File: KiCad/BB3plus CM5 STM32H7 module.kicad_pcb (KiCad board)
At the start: 6 copper layers, 55 x 40 mm, 134 parts, among them IC1 AZ1117CH2-3.3TRG1, IC10 MX25UM25645GXDI00-T, IC2 SN74LVC1G14DBVR, IC3 STM32H7R7L8H6H, IC4 TLV75718PDRVR, IC5 MX52LM04A11XVW, IC6 LAN8742A-CZ-TR, IC7 APS256XXN-OBR-BG, IC8 TFP410PAP, IC9 TS3DV642A0RUAR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

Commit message: DIN3 pin assigned
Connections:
- net UART0_RX/DIN2 renamed UART_RX/DIN2
- net UART0_TX/DOUT3 renamed UART_TX/DOUT3
- net UART1_RX/DIN1 renamed RS485_RX/DIN1
- net UART1_TX/DOUT1 renamed RS485_TX/DOUT1
- IC3 pad B6: unconnected-(IC3A-PD7-PadB6) -> DIN3
- SoM1 pad 35: unconnected-(SoM1A-ID_SC/GPIO1-Pad35) -> DIN3
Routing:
- net DIN3: track 0.00 -> 27.8 mm, vias 0 -> 5
- net SCL: track 73.0 -> 73.6 mm

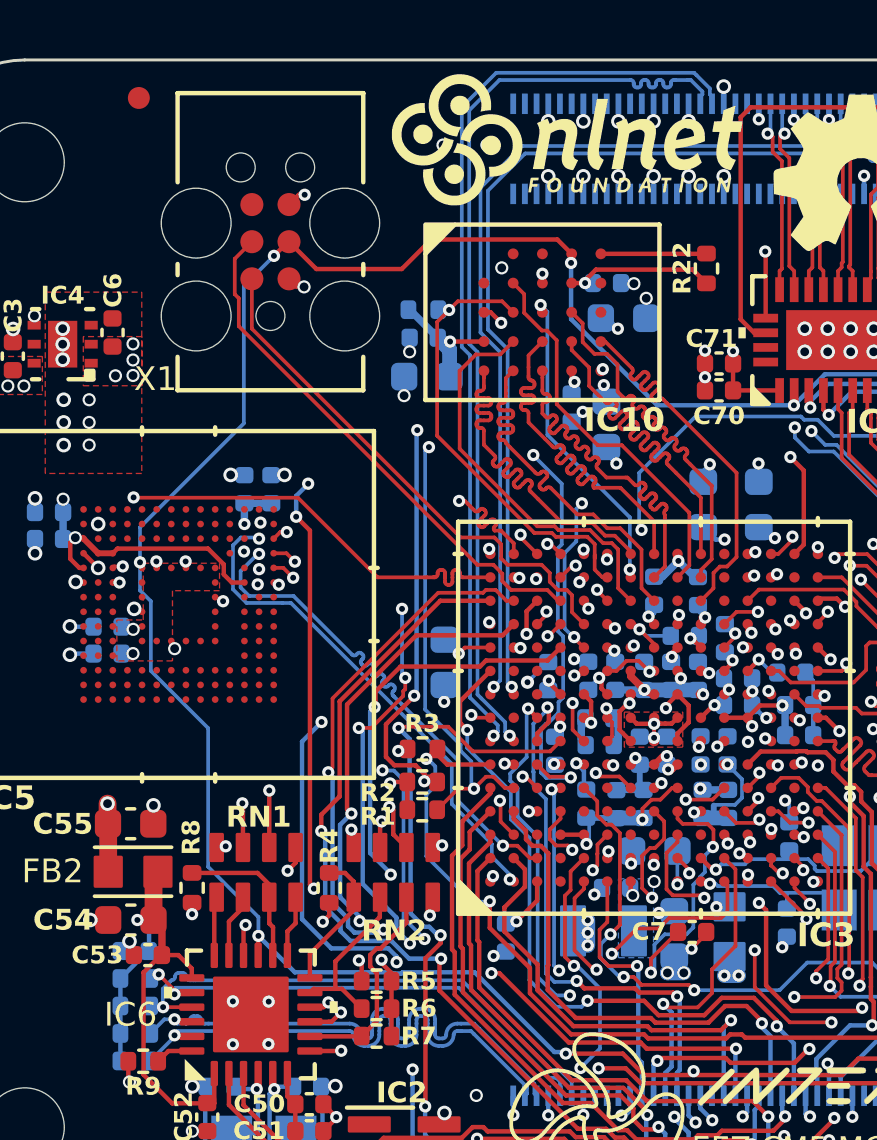
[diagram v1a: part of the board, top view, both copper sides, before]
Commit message: ETH clk fixed, digital I/O naming updated
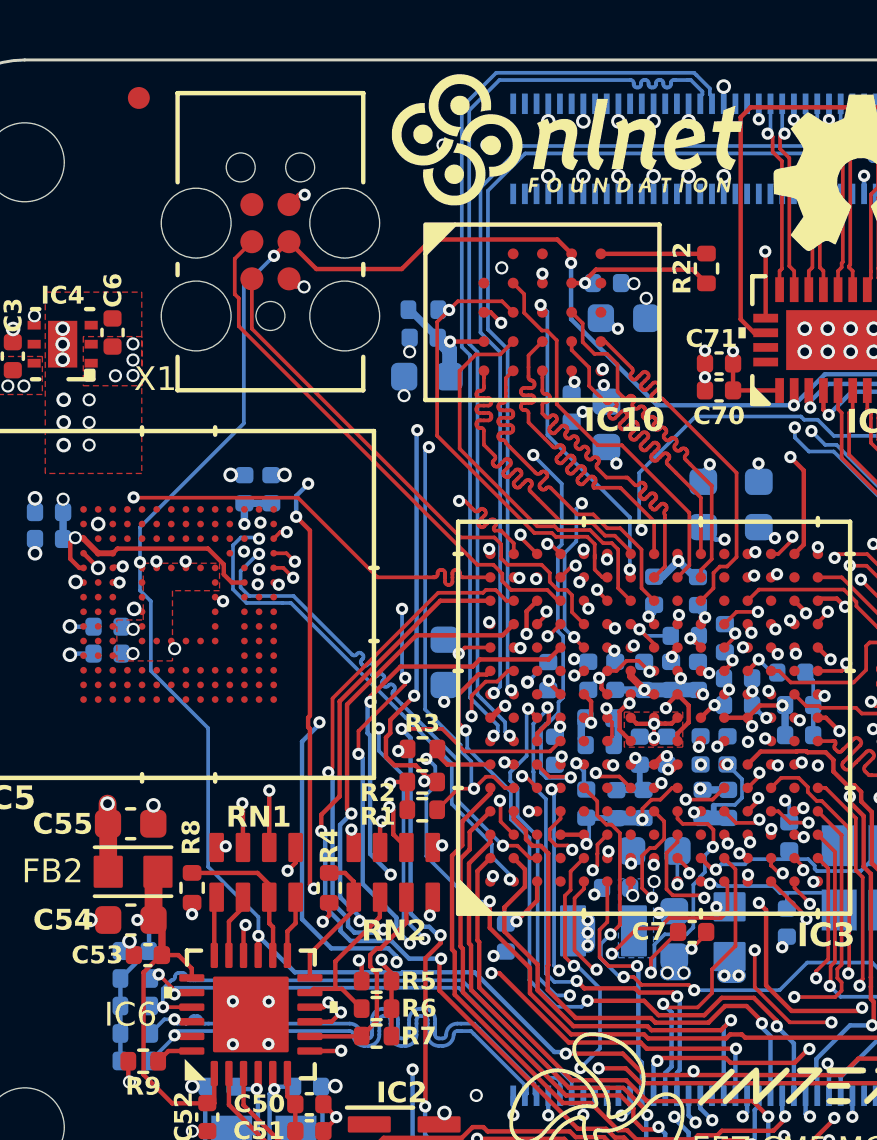
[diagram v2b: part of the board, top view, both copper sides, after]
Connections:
- net RS485_RX/DIN1 renamed RS485_RX/DIN3
- net RS485_TX/DOUT1 renamed RS485_TX/DOUT3
- net UART_RX/DIN2 renamed UART_RX/DIN1
- net UART_TX/DOUT3 renamed UART_TX/DOUT1
- IC3 pad B10: unconnected-(IC3B-PM2-PadB10) -> DIN2
- IC3 pad B6: DIN3 -> ETH_REF_CLK
- IC3 pad E7: ETH_REF_CLK -> unconnected-(IC3A-PD6-PadE7)
- SoM1 pad 35: DIN3 -> DIN2
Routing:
- net DIN2: track 0.00 -> 30.3 mm, vias 0 -> 5
- net DIN3: track 27.8 -> 0.00 mm, vias 5 -> 0
- net ETH_REF_CLK: track 15.7 -> 11.7 mm

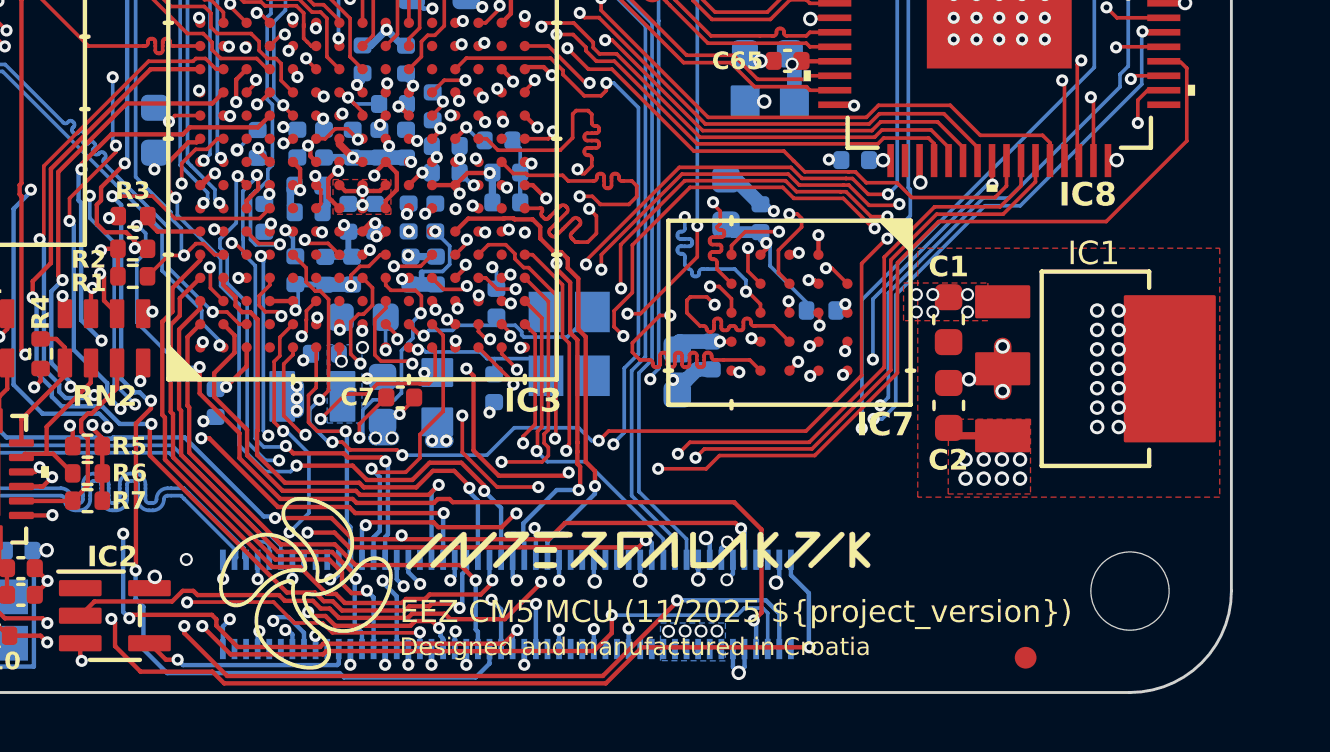
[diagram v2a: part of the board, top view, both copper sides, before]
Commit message: RTC input added
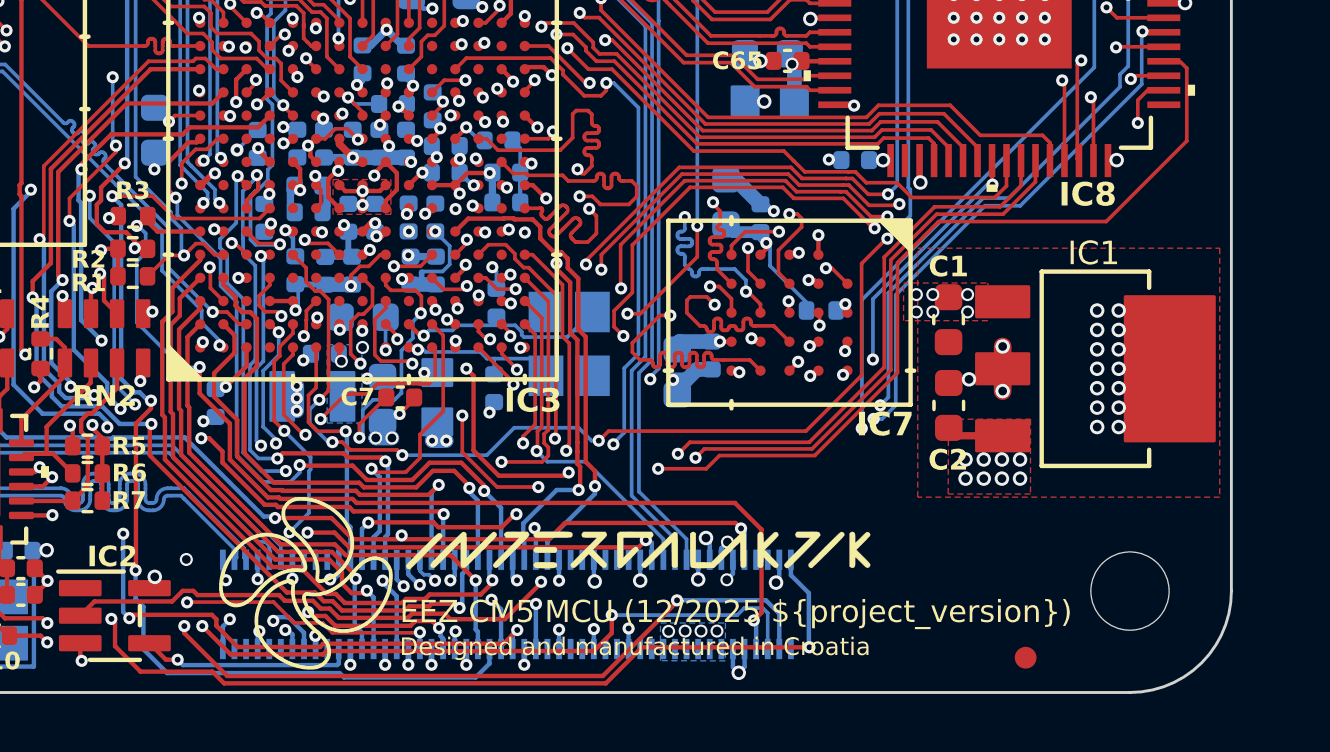
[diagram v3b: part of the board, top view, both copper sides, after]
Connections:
- IC3 pad D2: unconnected-(IC3A-PC14-OSC32_I_N-PadD2) -> RTC_CM5
- SoM1 pad 36: unconnected-(SoM1A-ID_SD/GPIO0-Pad36) -> RTC_CM5
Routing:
- net RTC_CM5: track 0.00 -> 13.7 mm, vias 0 -> 3
- net ~{DIB3_CSA}: track 24.7 -> 25.4 mm
- net ~{LED_PWR}: track 49.1 -> 48.3 mm
- net DIB4_MOSI: track 19.1 -> 19.7 mm
- net ~{DIB4_IRQ}: track 17.7 -> 18.2 mm
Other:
- board text added: "EEZ CM5 MCU (12/2025 ${project_version})"
- board text removed: "EEZ CM5 MCU (11/2025 ${project_version})"
